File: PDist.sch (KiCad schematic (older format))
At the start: 55 parts

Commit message: Squiggles! Silk!
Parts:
- renumbered C10 to C1001, C11 to C1002, C12 to C1003, C13 to C1004, C14 to C1005, C15 to C1006, C16 to C1007, C17 to C1008, C18 to C1009, C19 to C1010, C20 to C1011, C21 to C1012, C22 to C1013, C23 to C1014, C24 to C1015, C25 to C1016, C26 to C1017, C27 to C1018, C28 to C1019, C29 to C1020, C30 to C1021, C31 to C1022, C32 to C1023, C90 to C1024, C91 to C1025, C79 to C1026, C92 to C1027, C93 to C1028, C94 to C1029, C95 to C1030, C80 to C1031, C96 to C1032, C97 to C1033, C81 to C1034, C146 to C1035, C147 to C1036, C148 to C1037, C149 to C1038, C150 to C1039, C151 to C1040, C183 to C1041, C152 to C1042, C153 to C1043, C154 to C1044, C155 to C1045, C156 to C1046, C157 to C1047, C158 to C1048, C159 to C1049, C160 to C1050, C161 to C1051

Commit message: Final BOM
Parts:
- C1001, C1002, C1003, C1004, C1005, C1006, C1007, C1008, C1009, C1010, C1011, C1012, C1013, C1014, C1015, C1016, C1017, C1018, C1019, C1020, C1021, C1022, C1023: value 100n -> 1u; BOM CAP MLCC 100n ≥X5R 25V 10% [0402] -> CAP MLCC 1u 6.3V 20% [0402]

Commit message: Fuck. Rip up bridge.
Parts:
- removed BRIDGE1: XC6SLX25-FGG484, manuf:XILINX-FGG484, symbol XC6SLX25-FGG484
- added BRIDGE1: XC6SLX45-FGG484, manuf:XILINX-FGG484, symbol XC6SLX45-FGG484
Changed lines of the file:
@@
-	1    0    0    -1
-$EndComp
-$Comp
-L XC6SLX25-FGG484 BRIDGE1
-U 5 1 576854D3
-P 4700 1000
-F 0 "BRIDGE1" H 5300 1268 50  0000 C CNN
-F 1 "XC6SLX25-FGG484" H 5300 1177 50  0000 C CNN
-F 2 "manuf:XILINX-FGG484" H 4800 1150 50  0001 C CNN
-F 3 "" H 4900 1250 60  0001 C CNN
-	5    4700 1000
 	1    0    0    -1
 $EndComp
@@
 Wire Wire Line
 	8100 9300 8100 9200
+$Comp
+L XC6SLX45-FGG484 BRIDGE1
+U 5 1 57B42599
+P 4700 1000
+F 0 "BRIDGE1" H 5300 1268 50  0000 C CNN
+F 1 "XC6SLX45-FGG484" H 5300 1177 50  0000 C CNN
+F 2 "manuf:XILINX-FGG484" H 4700 1300 50  0001 C CNN
+F 3 "" H 4700 1000 50  0001 C CNN
+	5    4700 1000
+	1    0    0    -1
+$EndComp
 $EndSCHEMATC

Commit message: Redecoupling
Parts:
- removed C1024, C1025, C1027, C1028, C1029, C1030, C1032, C1033, C1035, C1036, C1037, C1038, C1039, C1040, C1042, C1043, C1044, C1045, C1046, C1047, C1048, C1049, C1050, C1051: 1u, IPC7351-Nominal:CAPC1005X55, symbol C-0402
- removed CPU0, CPU1: XC6SLX25-FGG484, manuf:XILINX-FGG484, symbol XC6SLX25-FGG484
- added C1024, C1025, C1027, C1028, C1029, C1030, C1032, C1033, C1035, C1036, C1037, C1038, C1039, C1040, C1042, C1043, C1044, C1045, C1046, C1047, C1048, C1049, C1050, C1051: 100n, IPC7351-Nominal:CAPC0603X33, symbol C-0201
- added C1052, C1053, C1054: 22u, IPC7351-Nominal:CAPC2012X70, symbol C-0805
- added CPU0, CPU1: XC6SLX45-FGG484, manuf:XILINX-FGG484, symbol XC6SLX45-FGG484
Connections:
- wire segments 501 -> 507

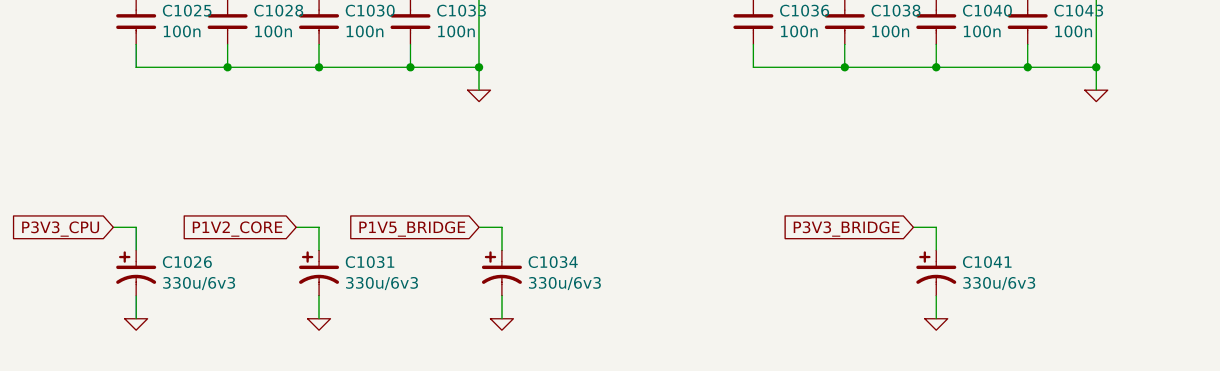
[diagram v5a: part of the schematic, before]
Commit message: Rearrange LEDs a bit, switch to al-poly caps
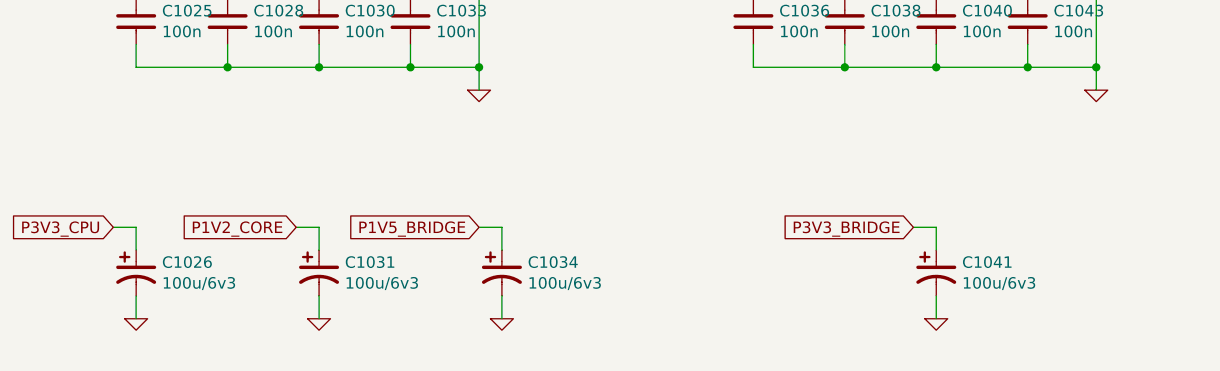
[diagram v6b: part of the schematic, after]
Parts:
- removed C1026, C1031, C1034, C1041: 330u/6v3, IPC7351-Nominal:CAPMP6032X280, symbol C-TANT-6032-28
- added C1026, C1031, C1034, C1041: 100u/6v3, IPC7351-Nominal:CAPAE530X540, symbol C-ALUM-530
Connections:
- net GND: now also C1026.2, C1031.2, C1034.2, C1041.2
- net P1V2_CORE: now also C1031.1
- net P1V5_BRIDGE: now also C1034.1
- net P3V3_BRIDGE: now also C1041.1
- net P3V3_CPU: now also C1026.1
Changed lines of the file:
@@
 Text GLabel 9300 2400 0    50   Input ~ 0
 P1V2_CORE
-$Comp
-L C-TANT-6032-28 C?
-U 1 1 5793D7F4
-P 4600 9100
-AR Path="/5765B2E6/5793D7F4" Ref="C?"  Part="1"
-AR Path="/5763AB3B/5793D7F4" Ref="C1026"  Part="1"
-F 0 "C1026" H 4713 9146 50  0000 L CNN
-F 1 "330u/6v3" H 4713 9055 50  0000 L CNN
-F 2 "IPC7351-Nominal:CAPMP6032X280" H 4600 8950 50  0001 C CNN
-F 3 "" H 4590 9075 60  0000 C CNN
-F 4 "DIST DIGIKEY 478-8902-1-ND" H 4600 8850 60  0001 C CNN "BOM"
-	1    4600 9100
-	1    0    0    -1
-$EndComp
 Text GLabel 4500 8900 0    50   Input ~ 0
 P3V3_CPU
@@
 P1V2_CORE
 $Comp
-L C-TANT-6032-28 C?
-U 1 1 57941170
-P 5400 9100
-AR Path="/5765B2E6/57941170" Ref="C?"  Part="1"
-AR Path="/5763AB3B/57941170" Ref="C1031"  Part="1"
-F 0 "C1031" H 5513 9146 50  0000 L CNN
-F 1 "330u/6v3" H 5513 9055 50  0000 L CNN
-F 2 "IPC7351-Nominal:CAPMP6032X280" H 5400 8950 50  0001 C CNN
-F 3 "" H 5390 9075 60  0000 C CNN
-F 4 "DIST DIGIKEY 478-8902-1-ND" H 5400 8850 60  0001 C CNN "BOM"
-	1    5400 9100
-	1    0    0    -1
-$EndComp
-$Comp
 L GND #PWR1007
 U 1 1 5794152A
@@
 P1V5_BRIDGE
 $Comp
-L C-TANT-6032-28 C?
-U 1 1 57941998
-P 6200 9100
-AR Path="/5765B2E6/57941998" Ref="C?"  Part="1"
-AR Path="/5763AB3B/57941998" Ref="C1034"  Part="1"
-F 0 "C1034" H 6313 9146 50  0000 L CNN
-F 1 "330u/6v3" H 6313 9055 50  0000 L CNN
-F 2 "IPC7351-Nominal:CAPMP6032X280" H 6200 8950 50  0001 C CNN
-F 3 "" H 6190 9075 60  0000 C CNN
-F 4 "DIST DIGIKEY 478-8902-1-ND" H 6200 8850 60  0001 C CNN "BOM"
-	1    6200 9100
-	1    0    0    -1
-$EndComp
-$Comp
 L GND #PWR1010
 U 1 1 57941D48
@@
 Text Notes 10050 7250 0    50   ~ 0
 CPU1 CORE
-$Comp
-L C-TANT-6032-28 C?
-U 1 1 57AD94B1
-P 8100 9100
-AR Path="/5765B2E6/57AD94B1" Ref="C?"  Part="1"
-AR Path="/5763AB3B/57AD94B1" Ref="C1041"  Part="1"
-F 0 "C1041" H 8213 9146 50  0000 L CNN
-F 1 "330u/6v3" H 8213 9055 50  0000 L CNN
-F 2 "IPC7351-Nominal:CAPMP6032X280" H 8100 8950 50  0001 C CNN
-F 3 "" H 8090 9075 60  0000 C CNN
-F 4 "DIST DIGIKEY 478-8902-1-ND" H 8100 8850 60  0001 C CNN "BOM"
-	1    8100 9100
-	1    0    0    -1
-$EndComp
 Text GLabel 8000 8900 0    50   Input ~ 0
 P3V3_BRIDGE
@@
 	6300 7700 6300 7600
 Connection ~ 6100 7700
+$Comp
+L C-ALUM-530 C1026
+U 1 1 57C83845
+P 4600 9100
+F 0 "C1026" H 4713 9146 50  0000 L CNN
+F 1 "100u/6v3" H 4713 9055 50  0000 L CNN
+F 2 "IPC7351-Nominal:CAPAE530X540" H 4600 9100 50  0001 C CNN
+F 3 "" H 4590 9075 60  0000 C CNN
+F 4 "DIST DIGIKEY 732-6394-1-ND" H 4600 9100 60  0001 C CNN "BOM"
+	1    4600 9100
+	1    0    0    -1
+$EndComp
+$Comp
+L C-ALUM-530 C1031
+U 1 1 57C84A06
+P 5400 9100
+F 0 "C1031" H 5513 9146 50  0000 L CNN
+F 1 "100u/6v3" H 5513 9055 50  0000 L CNN
+F 2 "IPC7351-Nominal:CAPAE530X540" H 5400 9100 50  0001 C CNN
+F 3 "" H 5390 9075 60  0000 C CNN
+F 4 "DIST DIGIKEY 732-6394-1-ND" H 5400 9100 60  0001 C CNN "BOM"
+	1    5400 9100
+	1    0    0    -1
+$EndComp
+$Comp
+L C-ALUM-530 C1034
+U 1 1 57C84ADC
+P 6200 9100
+F 0 "C1034" H 6313 9146 50  0000 L CNN
+F 1 "100u/6v3" H 6313 9055 50  0000 L CNN
+F 2 "IPC7351-Nominal:CAPAE530X540" H 6200 9100 50  0001 C CNN
+F 3 "" H 6190 9075 60  0000 C CNN
+F 4 "DIST DIGIKEY 732-6394-1-ND" H 6200 9100 60  0001 C CNN "BOM"
+	1    6200 9100
+	1    0    0    -1
+$EndComp
+$Comp
+L C-ALUM-530 C1041
+U 1 1 57C84BB9
+P 8100 9100
+F 0 "C1041" H 8213 9146 50  0000 L CNN
+F 1 "100u/6v3" H 8213 9055 50  0000 L CNN
+F 2 "IPC7351-Nominal:CAPAE530X540" H 8100 9100 50  0001 C CNN
+F 3 "" H 8090 9075 60  0000 C CNN
+F 4 "DIST DIGIKEY 732-6394-1-ND" H 8100 9100 60  0001 C CNN "BOM"
+	1    8100 9100
+	1    0    0    -1
+$EndComp
 $EndSCHEMATC
